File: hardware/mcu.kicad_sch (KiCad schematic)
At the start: 2 parts, among them U1 NUCLEO-H503RB, U2 SN74LVC1T45DBV

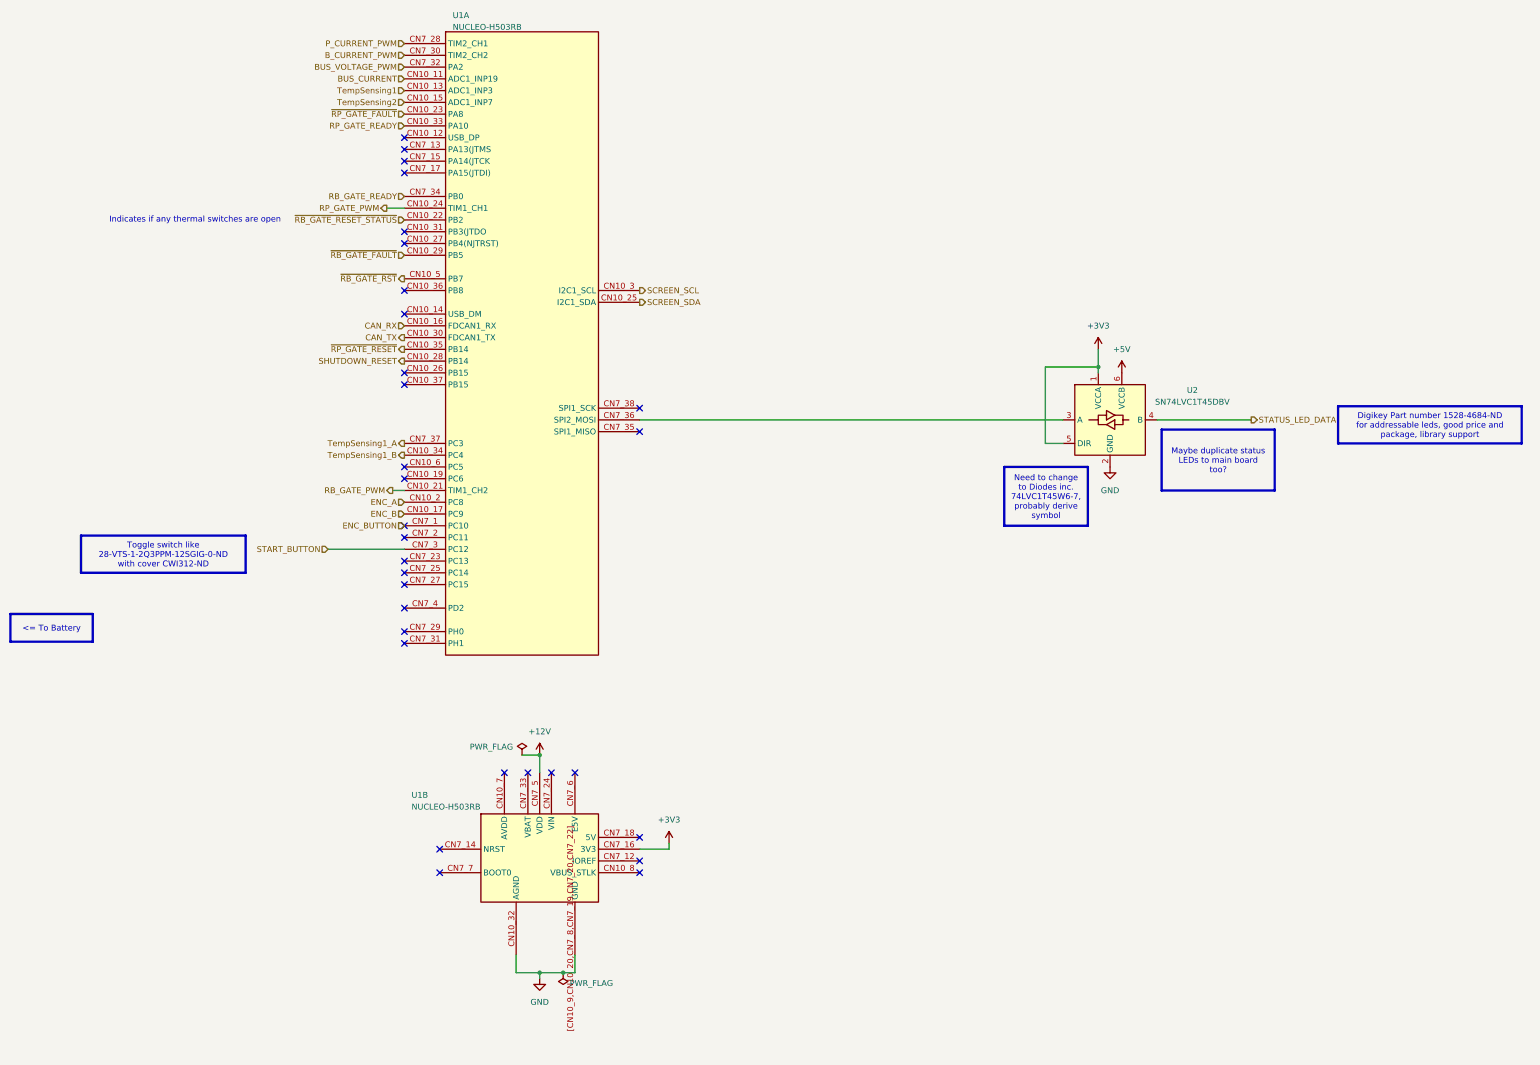
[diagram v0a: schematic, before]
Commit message: Finished Layout and routing
* Flipped CAN transceiver upside down on schematic
* Moved CAN transceiver nearer to J13 and MCU CAN pins
* Moved 5V DCDC caps nearer to 5V DCDC
* Moved Silkscreen out from under U9
* Moved J2 and J1 to prevent plugging 12V into a temp sensor connector
* Change +3.3V to +3V3 to match MCU page
* Changed Current Sense circuit to use U4D, sharing with Temp Sense (for easier assembly)
* Placed Unused MCP6004s on schematic and connected them per datasheet fig 4-5
* Remove connections to HV- in Current Sensing (Replaced with GND)
* Tightened up Temp and Current Sense amplifier layouts
* Swap U15A with U15D for easier routing
* Added buffer to voltage sense circuit because filter stage could significantly load the voltage divider
* Added a smattering of decoupling caps
* Finished Layout and routing
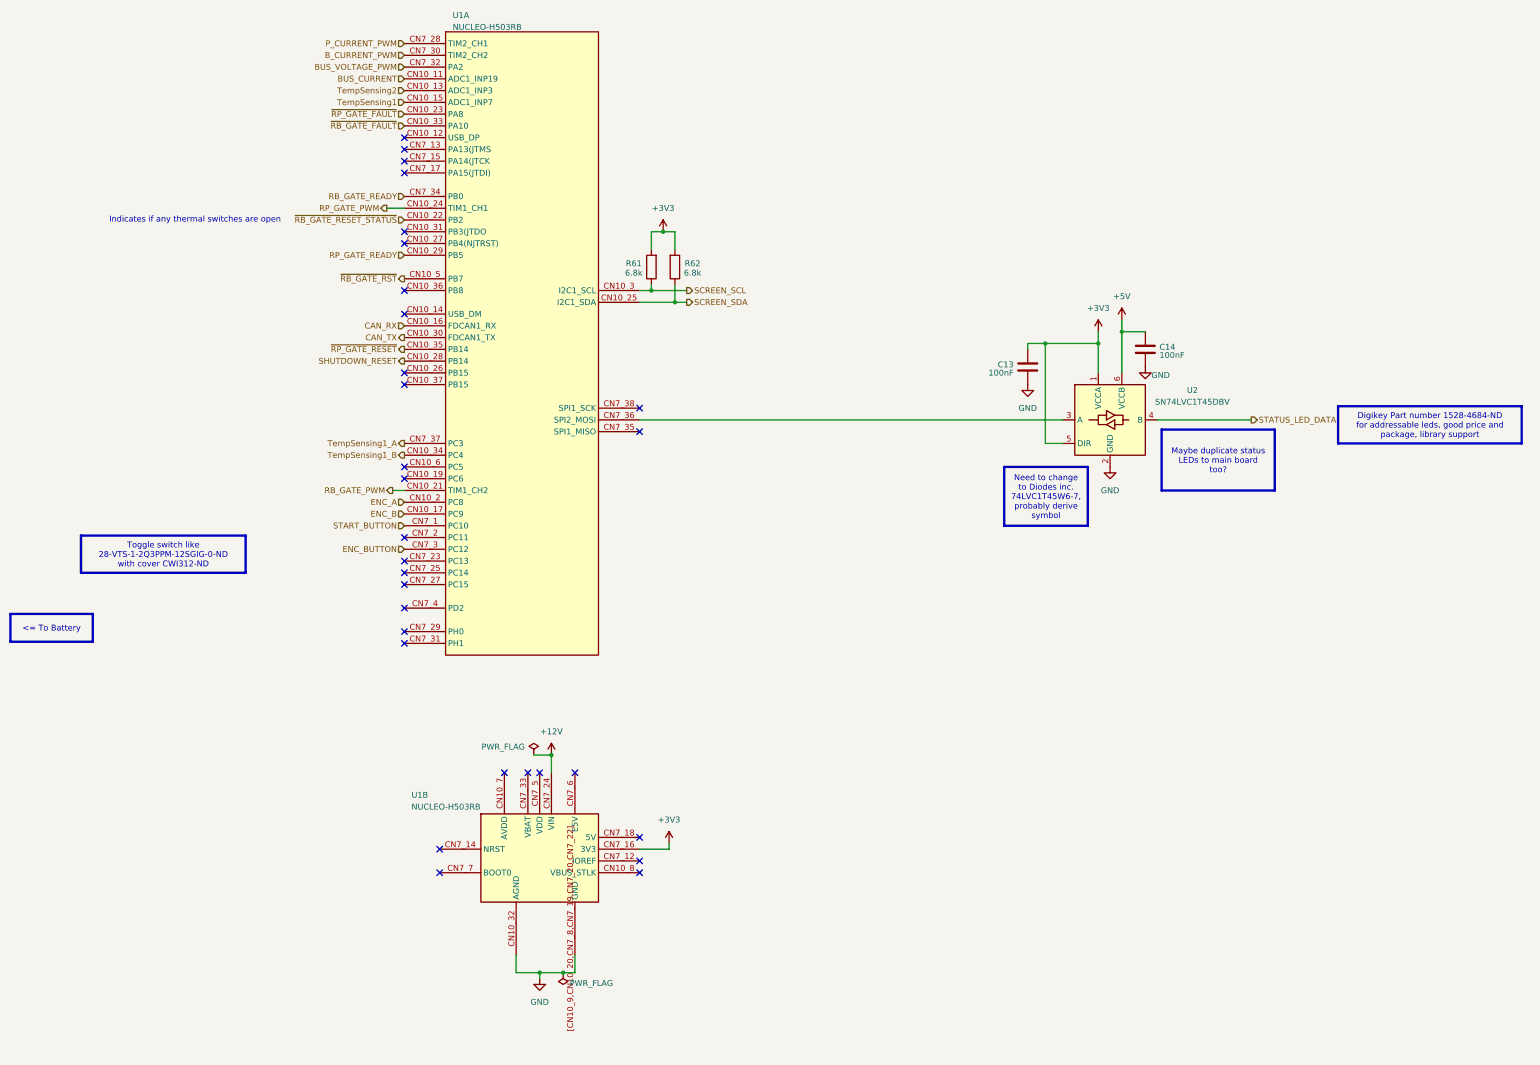
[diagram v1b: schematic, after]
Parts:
- added C13, C14: 100nF, Capacitor_SMD:C_0805_2012Metric_Pad1.18x1.45mm_HandSolder, symbol Device:C
- added R61, R62: 6.8k, Resistor_SMD:R_0805_2012Metric_Pad1.20x1.40mm_HandSolder, symbol Device:R
- U2: KiLib_Generator (none) -> package/gullwing
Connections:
- net +12V: now also U1.CN7_24 (VIN); no longer U1.CN7_5 (VDD)
- net +3V3: now also C13.1, R61.2, R62.2
- net +5V: now also C14.1
- net ENC_BUTTON: now also U1.CN7_3 (PC12); no longer U1.CN7_1 (PC10)
- net GND: now also C13.2, C14.2
- net RP_GATE_READY: now also U1.CN10_29 (PB5); no longer U1.CN10_33 (PA10)
- net SCREEN_SCL: now also R61.1
- net SCREEN_SDA: now also R62.1
- net START_BUTTON: now also U1.CN7_1 (PC10); no longer U1.CN7_3 (PC12)
- net TempSensing1: now also U1.CN10_15 (PA7); no longer U1.CN10_13 (PA6)
- net TempSensing2: now also U1.CN10_13 (PA6); no longer U1.CN10_15 (PA7)
- net ~{RB_GATE_FAULT}: now also U1.CN10_33 (PA10); no longer U1.CN10_29 (PB5)
- no-connect marks 31 -> 30
